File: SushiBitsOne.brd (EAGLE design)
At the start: 68.6 x 53.3 mm, 57 parts, among them IC1 CH340B, IC2 LM3671-3.3DBV, IC3 TPS562200DBV, J1 ARDUINO_R3, J2 DC-005, Q1 2N7002, Q2 MMBT2222A, U1 STM32F103CBT6-LQFP48, X1 32768Hz, X2 8MHz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

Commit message: Release: M193v3
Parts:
- added L3: (no value), rcl:L2012C
- X1: device Seeed-OPL-crystal-osctllator:X2-2.0-D9.1XL3.3MM -> SparkFun-Clocks:CRYSTAL-SMD-3.2X1.5MM
- X2: device Seeed-OPL-crystal-osctllator:HC49US -> SparkFun-Clocks:CRYSTAL-SMD-5X3.2-4PAD
- X3: device con-molex:87758-1016 -> con-leotronics:1365-10
- moved C8 15.0 mm to (43.5, 19.7), turned to 270 degrees
- moved C6 14.5 mm to (55.6, 28.6), turned to 90 degrees
- moved C3 4.13 mm to (36.2, 26.4), turned to 180 degrees
- moved C4 4.02 mm to (31.1, 23.5)
- moved X3 1.42 mm to (60.3, 41.0)
- moved X2 1.42 mm to (35.2, 23.5), turned to 180 degrees
- moved X1 0.64 mm to (41.0, 25.4)
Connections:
- new net N$20: C8.1, L3.2, U1.9
- net +3V3: now also L3.1; no longer C8.1, U1.9
- net HSEOUT: now also X2.3; no longer X2.2
- net LSEIN: now also X1.P$1; no longer X1.1
- net LSEOUT: now also X1.P$2; no longer X1.2
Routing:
- net N$20: track 0.00 -> 5.95 mm
- net +3V3: track 114.4 -> 111.0 mm, vias 10 -> 11
- net HSEIN: track 15.4 -> 12.0 mm
- net JTMS: track 23.4 -> 26.0 mm, vias 1 -> 2
- net JTCK: track 23.8 -> 26.1 mm, vias 1 -> 2
- net RESET#: track 88.9 -> 91.0 mm
- net JTDO: track 26.9 -> 28.8 mm, vias 1 -> 2
- net JTDI: track 28.2 -> 29.8 mm, vias 1 -> 2
- net HSEOUT: track 15.8 -> 16.9 mm
- net N$12: track 32.2 -> 31.5 mm
- net GND: vias 35 -> 38
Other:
- board text added: "SushiBits M193v3"
- board text removed: "SushiBits M193v2"

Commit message: Adjusting for the v4
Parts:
- moved X3 0.64 mm to (59.7, 41.0)
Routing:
- net UD-: track 60.9 -> 62.1 mm
- net D12: track 50.4 -> 49.5 mm
- net JTMS: track 26.0 -> 25.3 mm
- net JTDO: track 28.8 -> 28.2 mm
- net JTDI: track 29.8 -> 29.2 mm
- net JTCK: track 26.1 -> 25.5 mm
- net +3V3: track 111.0 -> 110.4 mm
- net D13: track 55.8 -> 55.3 mm

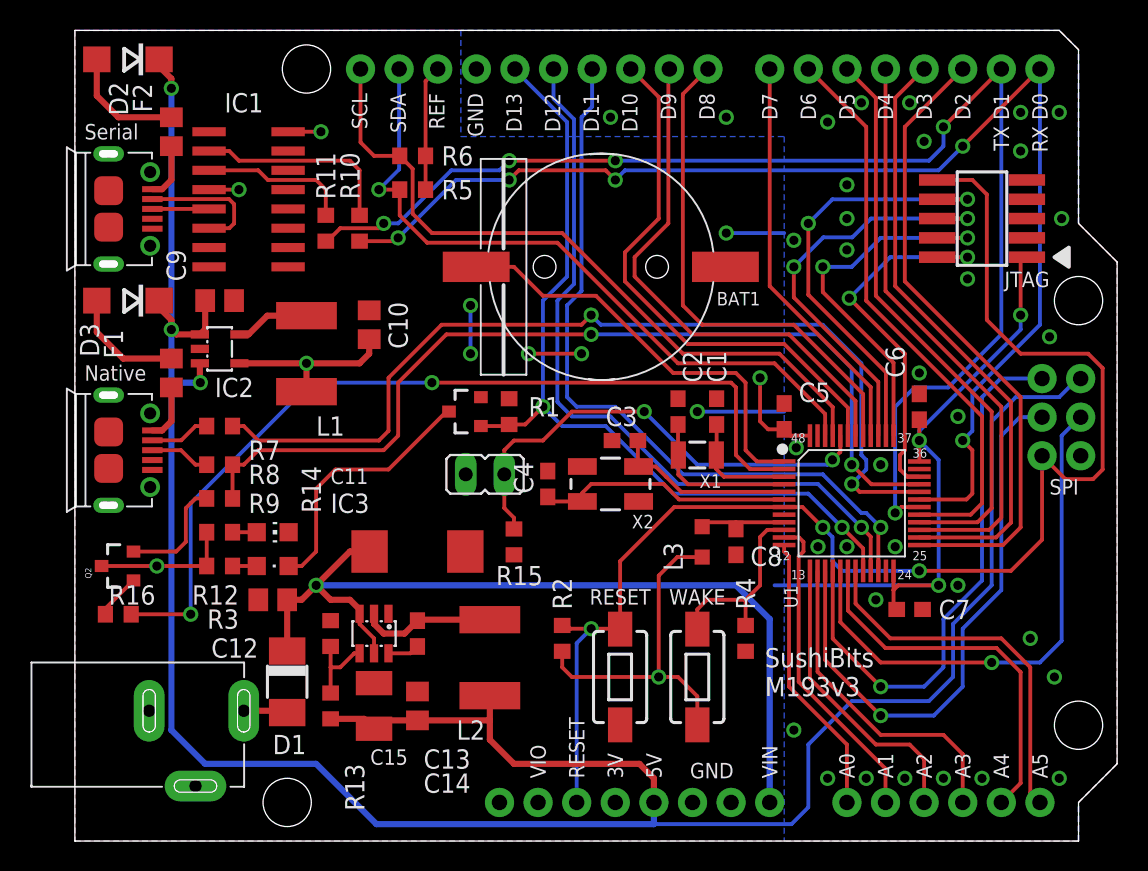
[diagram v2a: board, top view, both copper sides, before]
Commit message: Implemented the USB microcontroller with USB-Serial and CMSIS-DAP.
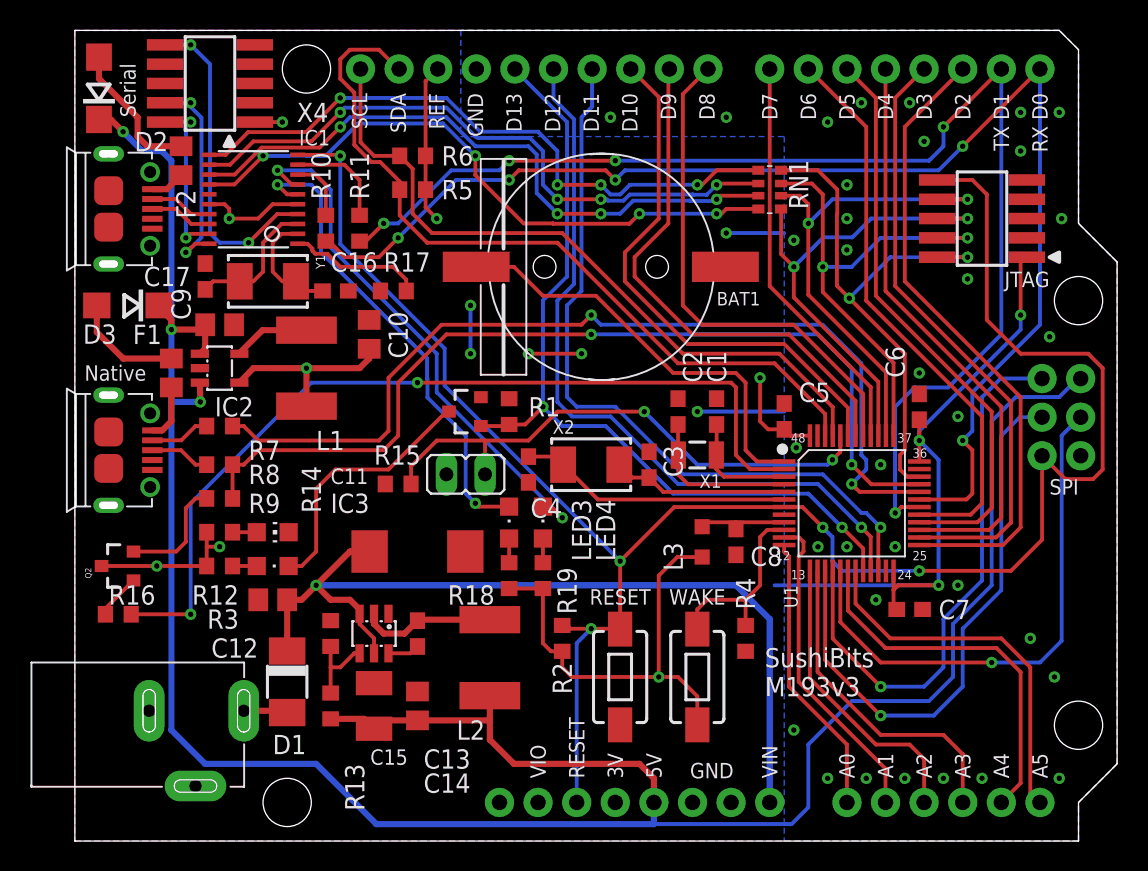
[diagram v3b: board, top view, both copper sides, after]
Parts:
- added C16, C17: 22p, rcl:C0603
- added LED3: Amber, led:CHIPLED_0805
- added LED4: Green, led:CHIPLED_0805
- added R17: 10k, rcl:R0603
- added R18, R19: 510, rcl:R0603
- added RN1: 510, resistor-dil:EXB38V
- added X4: 1365-10, con-leotronics:1365-10
- added Y1: (no value), SparkFun-Clocks:CRYSTAL-SMD-5X3.2-2PAD
- IC1: value CH340B -> STM32F042F6P6; device WCH:SO16 -> HeadphoneBT:TSSOP20
- X2: device SparkFun-Clocks:CRYSTAL-SMD-5X3.2-4PAD -> SparkFun-Clocks:CRYSTAL-SMD-5X3.2-2PAD
- moved R15 8.52 mm to (21.3, 23.5), turned to 0 degrees
- moved D2 2.69 mm to (1.59, 49.5), turned to 90 degrees
- moved C3 2.25 mm to (37.8, 24.8), turned to 90 degrees
- moved R10 2.22 mm to (16.5, 40.3)
- moved R11 2.22 mm to (18.7, 40.3)
- moved F2 2.01 mm to (6.99, 44.8)
- moved X2 1.80 mm to (34.0, 24.8), turned to 0 degrees
- moved C9 1.59 mm to (9.53, 34.0)
- moved C4 1.59 mm to (29.8, 24.4), turned to 270 degrees
- moved IC2 1.27 mm to (9.53, 31.1)
- moved JP1 1.27 mm to (25.7, 24.1)
- moved L1 0.95 mm to (15.2, 31.1)
- moved C10 0.63 mm to (19.4, 33.3)
- moved D3 0.32 mm to (3.49, 35.2)
- moved IC1 0.32 mm to (11.7, 42.2), turned to 90 degrees
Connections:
- new net N$21: IC1.8, R10.1
- new net N$22: IC1.9, R11.1
- new net N$23: IC1.4, X4.10
- new net N$24: IC1.19, X4.2
- new net N$25: IC1.20, X4.4
- new net N$26: IC1.1, R17.2
- new net N$27: IC1.6, LED3.C
- new net N$28: IC1.7, LED4.C
- new net N$29: LED3.A, R18.1
- new net N$30: LED4.A, R19.1
- new net TCK: IC1.12, RN1.2
- new net TDI: IC1.13, RN1.3
- new net TDO: IC1.14, RN1.4
- new net TMS: IC1.11, RN1.1
- net +3V3: now also IC1.5, R18.2, R19.2, X4.1; no longer IC1.4
- net GND: now also C16.2, C17.2, IC1.15, R17.1, X4.3, X4.5, X4.9; no longer IC1.1
- net HSEIN: now also X2.P$1; no longer X2.1
- net HSEOUT: now also X2.P$2; no longer X2.3
- net JTCK: now also RN1.7
- net JTDI: now also RN1.6
- net JTDO: now also RN1.5
- net JTMS: now also RN1.8
- net N$3: now also IC1.17; no longer IC1.6
- net N$4: now also IC1.18; no longer IC1.5
- net N$5: now also C16.1, Y1.P$1; no longer R10.1
- net N$6: now also C17.1, Y1.P$2; no longer R11.1
- net RESET#: now also IC1.10
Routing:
- net TDI: track 0.00 -> 42.3 mm, vias 0 -> 4
- net TMS: track 0.00 -> 42.3 mm, vias 0 -> 4
- net TCK: track 0.00 -> 42.0 mm, vias 0 -> 4
- net TDO: track 0.00 -> 41.7 mm, vias 0 -> 4
- net RESET#: track 91.2 -> 128.3 mm, vias 3 -> 5
- net N$28: track 0.00 -> 35.2 mm, vias 0 -> 2
- net N$27: track 0.00 -> 31.6 mm, vias 0 -> 2
- net N$23: track 0.00 -> 21.4 mm, vias 0 -> 2
- net +3V3: track 110.4 -> 126.2 mm, vias 11 -> 13
- net N$25: track 0.00 -> 14.0 mm, vias 0 -> 2
- net JTMS: track 25.3 -> 37.0 mm
- net N$24: track 0.00 -> 11.1 mm, vias 0 -> 2
- net N$26: track 0.00 -> 8.94 mm
- net JTCK: track 25.5 -> 33.3 mm
- net N$22: track 0.00 -> 6.81 mm
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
